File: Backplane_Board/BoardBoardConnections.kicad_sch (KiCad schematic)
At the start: 32 parts, among them J27 Conn_01x03_Pin, J28 Conn_01x03_Pin, J29 Conn_01x03_Pin, J30 BM03B-SRSS-TB, J31 Conn_01x04, J32 Conn_01x05_Socket, J33 BM03B-SRSS-TB, J34 Connector_PinHeader_2.54mm:Pi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, J35 Connector_PinHeader_2.54mm:Pi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, J36 Conn_01x03_Pin, Q3 SI7615ADN-T1-GE3, U6 Pico

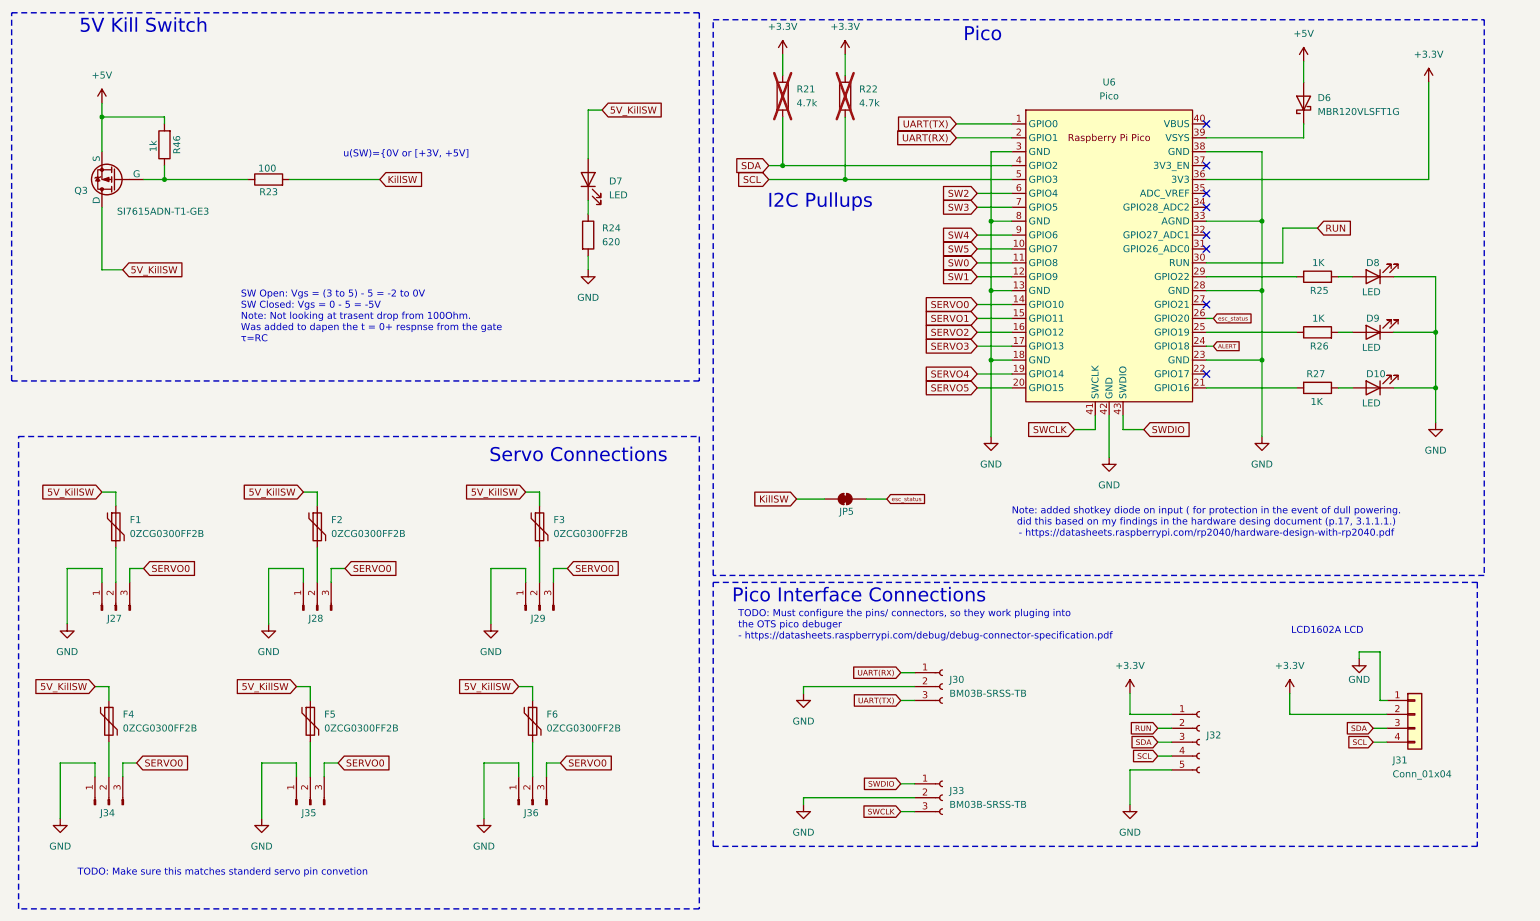
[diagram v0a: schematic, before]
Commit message: rough layout compleat, 200+ drc errors to fix
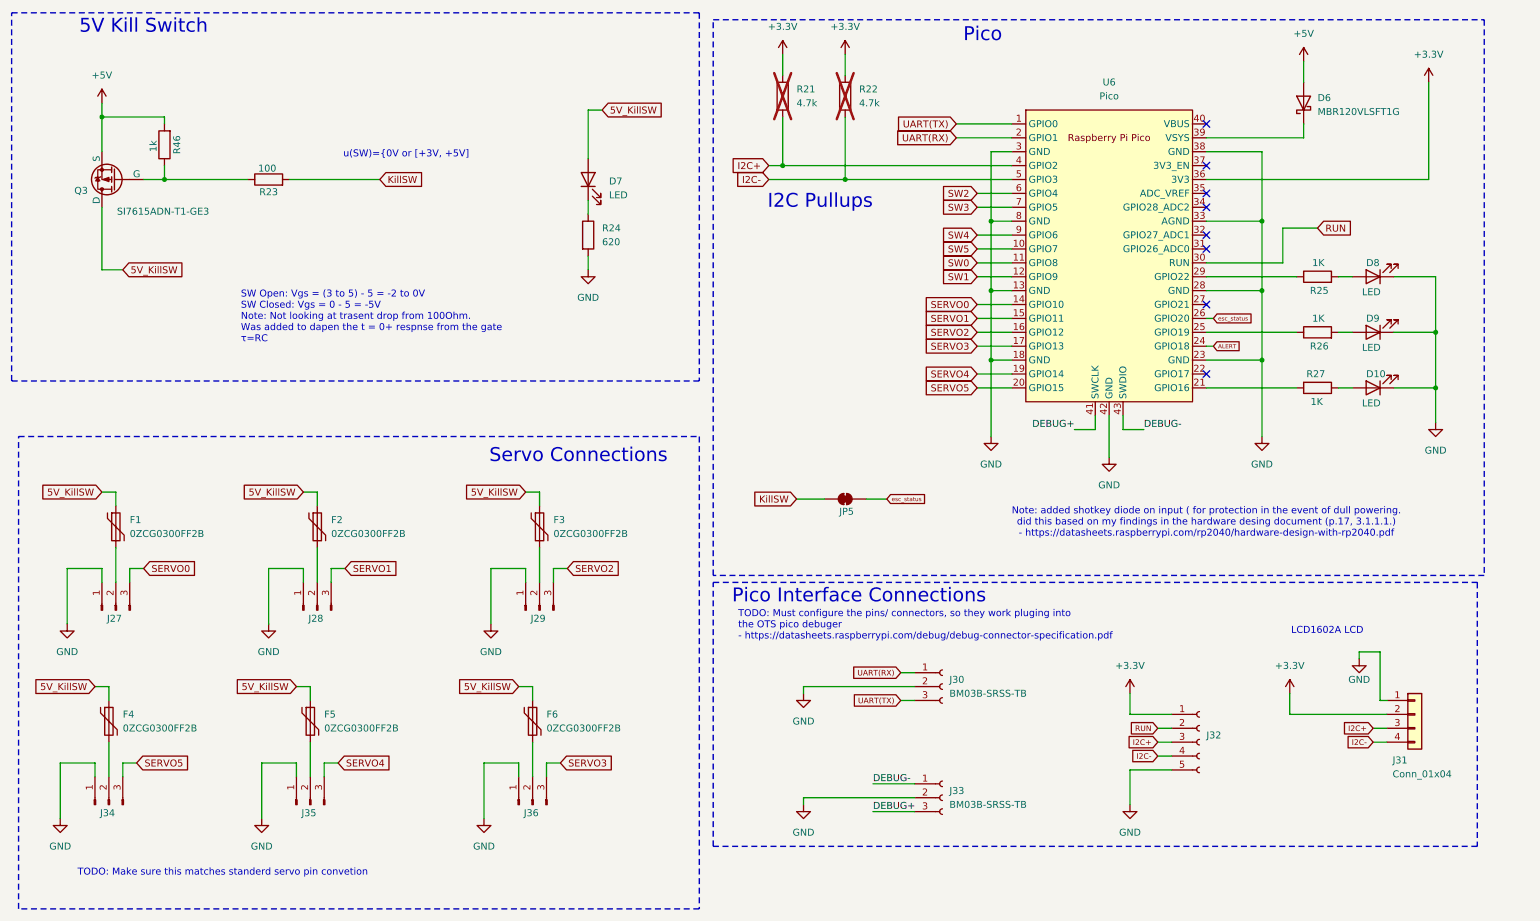
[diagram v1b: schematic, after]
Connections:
- net SERVO0: no longer J28.3 (Pin_3), J29.3 (Pin_3), J34.3 (Pin_3), J35.3 (Pin_3), J36.3 (Pin_3)
- net SERVO1: now also J28.3 (Pin_3)
- net SERVO2: now also J29.3 (Pin_3)
- net SERVO3: now also J36.3 (Pin_3)
- net SERVO4: now also J35.3 (Pin_3)
- net SERVO5: now also J34.3 (Pin_3)
- net SCL renamed I2C-
- net SDA renamed I2C+
- net SWCLK renamed DEBUG+
- net SWDIO renamed DEBUG-

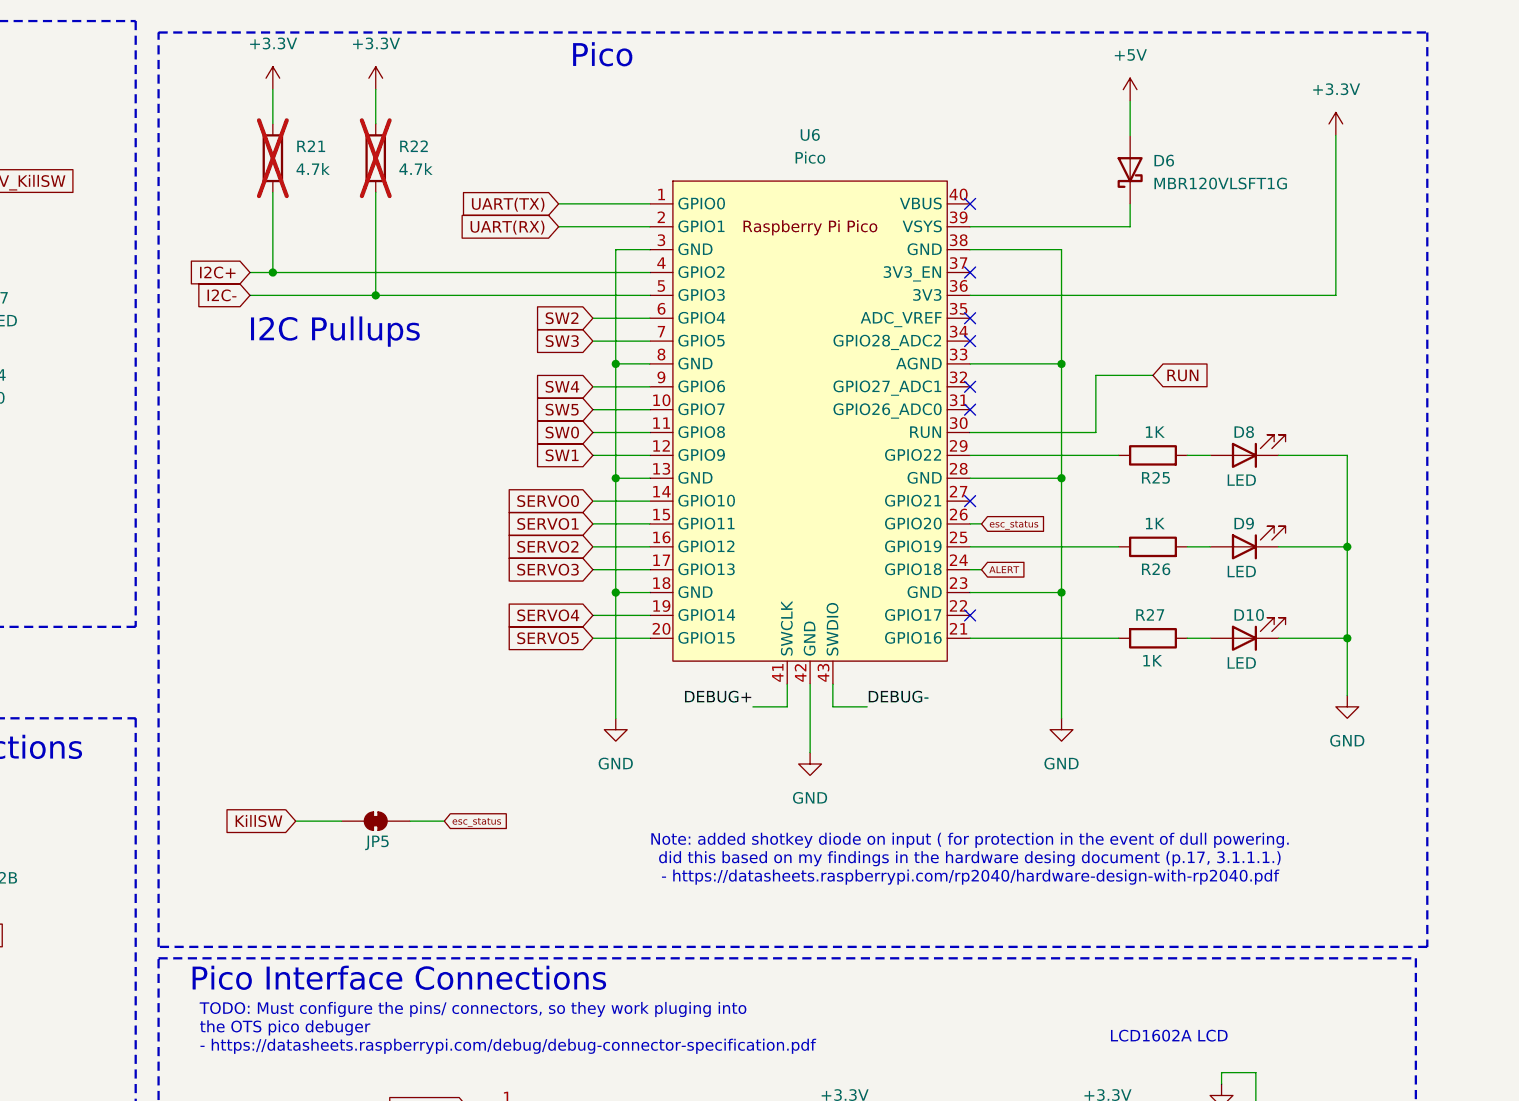
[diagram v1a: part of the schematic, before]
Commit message: added sd card, more drc stuff to fix
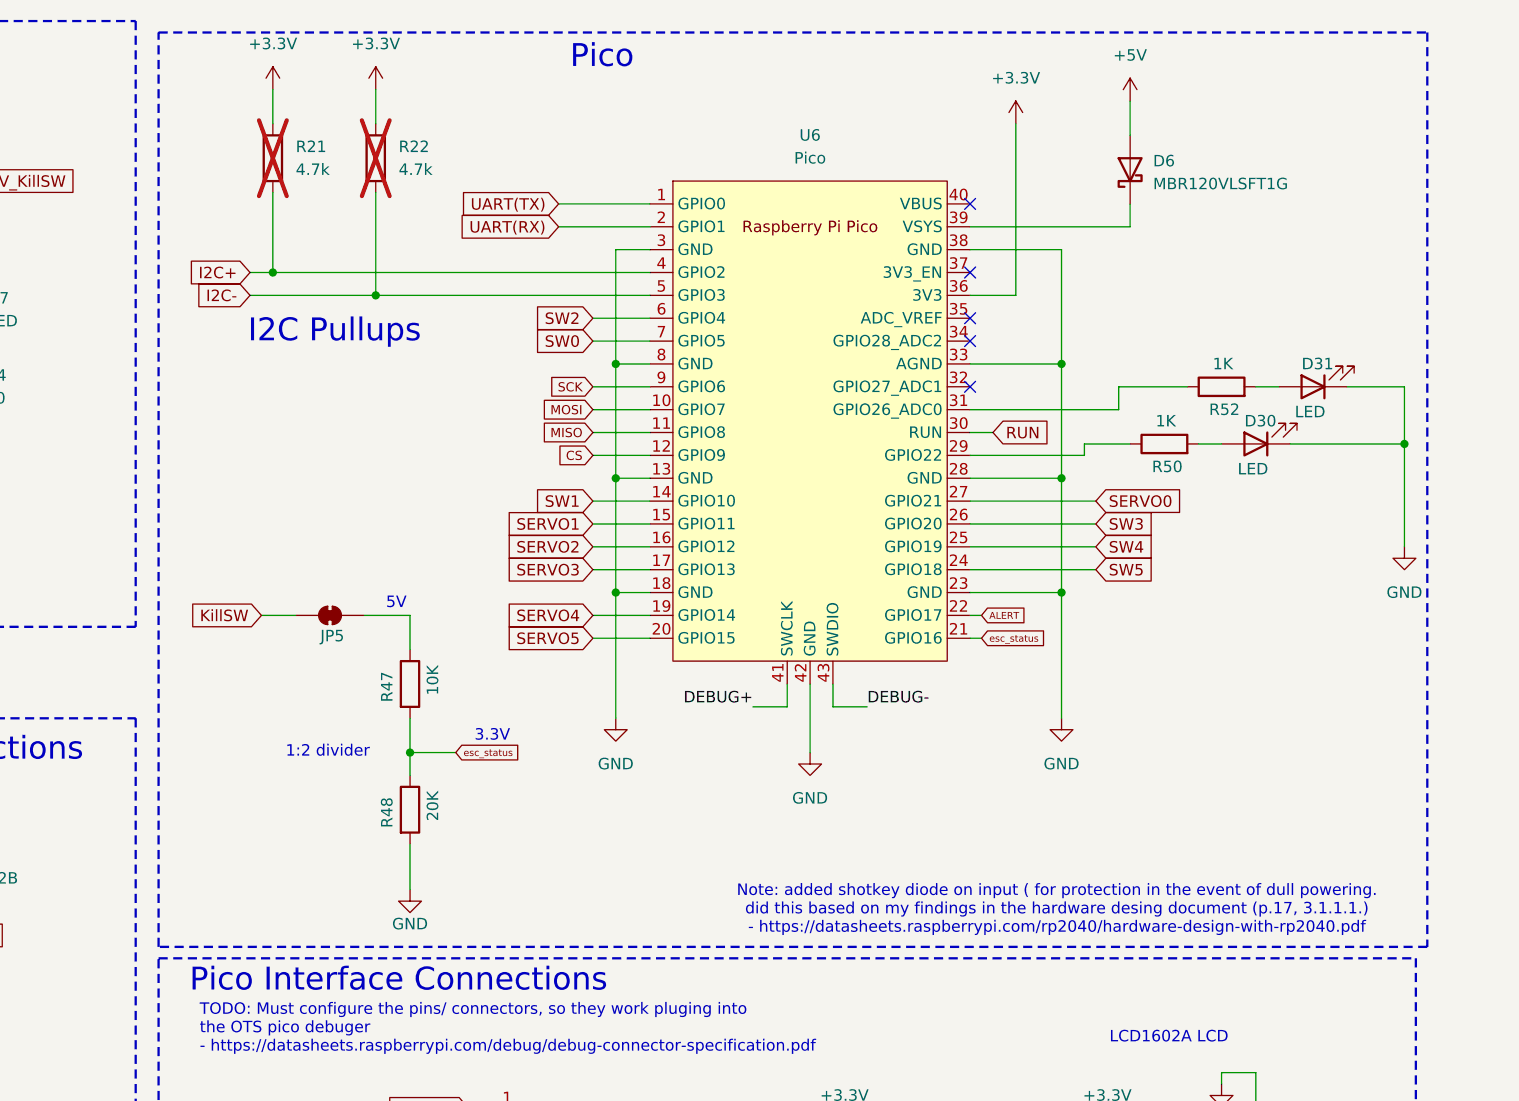
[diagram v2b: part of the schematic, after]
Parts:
- removed D10, D8, D9: LED, LED_SMD:LED_0603_1608Metric, symbol Device:LED
- removed R25, R26, R27: 1K, Resistor_SMD:R_0805_2012Metric_Pad1.20x1.40mm_HandSolder, symbol Device:R
- added D30, D31: LED, LED_SMD:LED_0603_1608Metric, symbol Device:LED
- added R47: 10K, Resistor_SMD:R_0805_2012Metric_Pad1.20x1.40mm_HandSolder, symbol Device:R
- added R48: 20K, Resistor_SMD:R_0805_2012Metric_Pad1.20x1.40mm_HandSolder, symbol Device:R
- added R50, R52: 1K, Resistor_SMD:R_0805_2012Metric_Pad1.20x1.40mm_HandSolder, symbol Device:R
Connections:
- net ALERT: now also U6.22 (GPIO17); no longer U6.24 (GPIO18)
- net GND: now also D30.1 (K), D31.1 (K), R48.2
- net SERVO0: now also U6.27 (GPIO21); no longer U6.14 (GPIO10)
- net SW0: now also U6.7 (GPIO5); no longer U6.11 (GPIO8)
- net SW1: now also U6.14 (GPIO10); no longer U6.12 (GPIO9)
- net SW3: now also U6.26 (GPIO20); no longer U6.7 (GPIO5)
- net SW4: now also U6.25 (GPIO19); no longer U6.9 (GPIO6)
- net SW5: now also U6.24 (GPIO18); no longer U6.10 (GPIO7)
- net esc_status: now also U6.21 (GPIO16), R47.2, R48.1; no longer JP5.1 (A), U6.26 (GPIO20)
- net at U6.29 (GPIO22): now also R50.1
- net at U6.31 (GPIO26_ADC0): now also R52.1
- new net: D30.2 (A), R50.2
- new net: JP5.1 (A), R47.1
- new net: D31.2 (A), R52.2
- new net CS: U6.12 (GPIO9)
- new net MISO: U6.11 (GPIO8)
- new net MOSI: U6.10 (GPIO7)
- new net SCK: U6.9 (GPIO6)
- no-connect marks 8 -> 5
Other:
- note added: "1:2 divider"
- note added: "3.3V"
- note added: "5V"
- moved on the sheet: JP5

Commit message: added gerber
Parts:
- R24: value 620 -> 1k
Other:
- note added: "2/3 divider"
- note removed: "1:2 divider"
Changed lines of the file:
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@@
 		)
 	)
-	(text "1:2 divider"
+	(text "2/3 divider"
 		(exclude_from_sim no)
 		(at 161.036 93.98 0)
@@
 			)
 		)
-		(property "Value" "620"
+		(property "Value" "1k"
 			(at 121.92 54.6099 0)
 			(effects
